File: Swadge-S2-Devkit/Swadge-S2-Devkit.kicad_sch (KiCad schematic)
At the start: 83 parts, among them J1 USB_B_Micro, J2 DEBUG_BANK_C, J3 DEBUG_BANK_B, J4 DEBUG_BANK_A, J5 MICSEL, J6 TRYMIC, M1 Motor_DC, Q1 Q_N_FET, Q2 AP2003_PN_FET, Q3 AP2003_PN_FET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

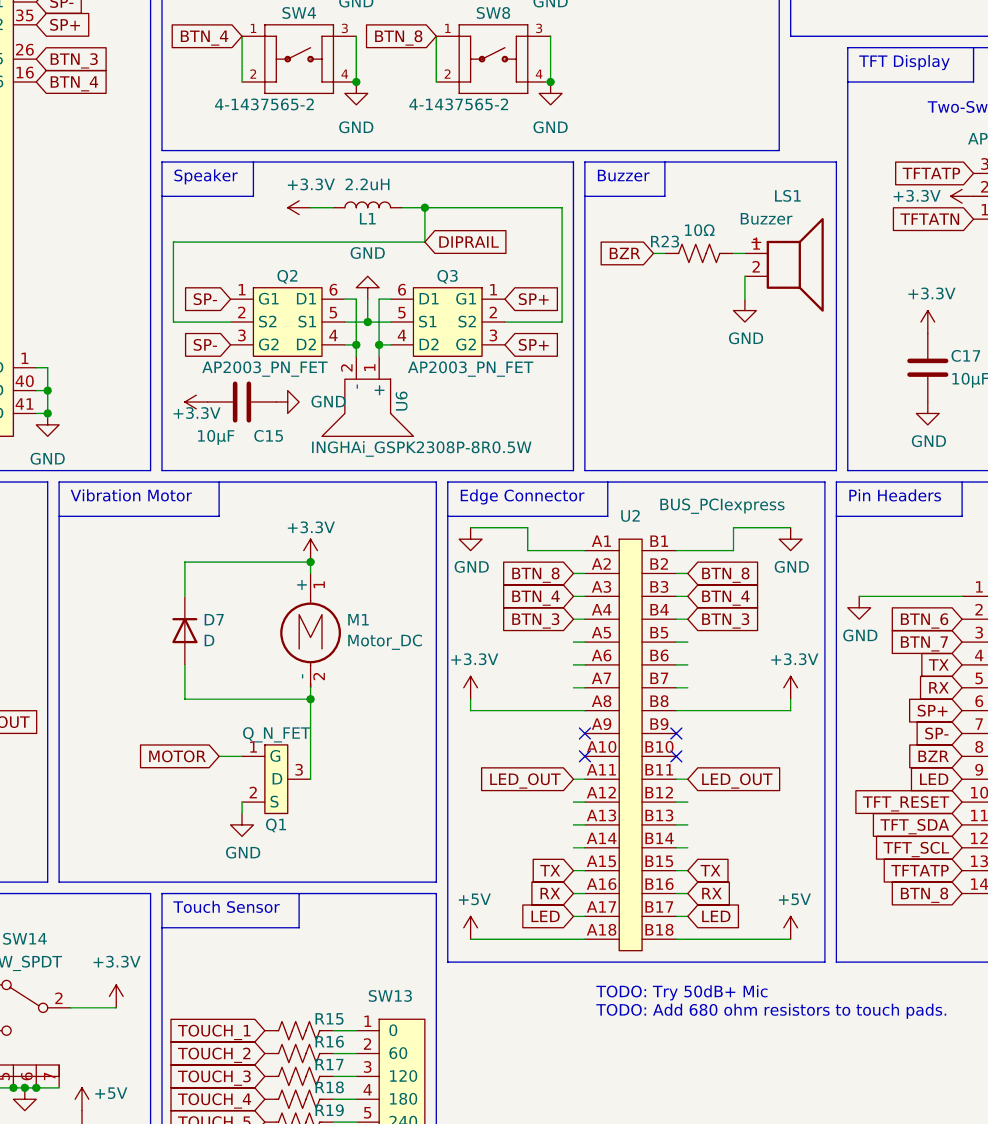
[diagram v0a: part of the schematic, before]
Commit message: Switched to controller PCB
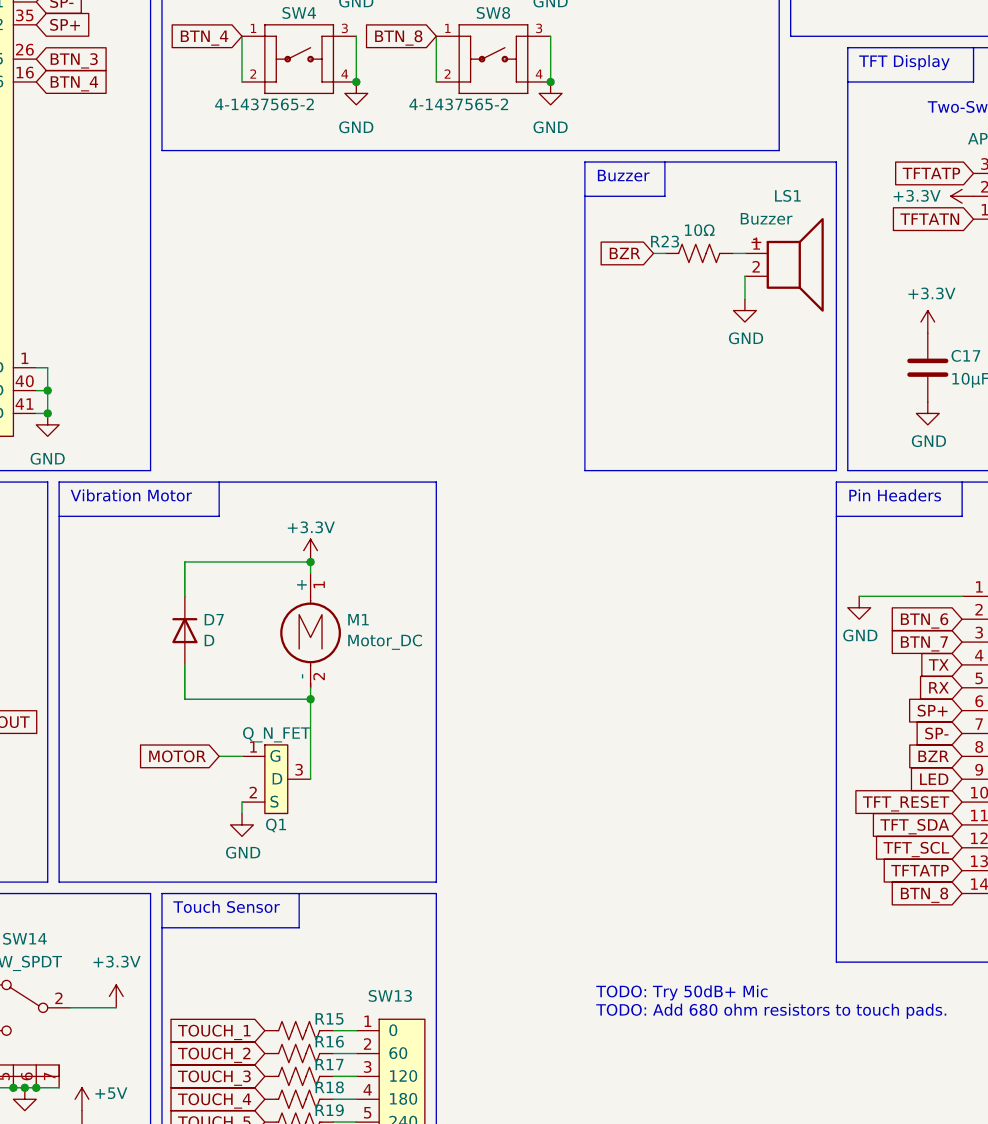
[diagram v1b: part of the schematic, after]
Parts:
- removed C15: 10μF, Swadge_Parts:C_0603_1608Metric, symbol Swadge_Parts:C
- removed L1: 2.2uH, Swadge_Parts:L_0603_1608Metric, symbol Swadge_Parts:L
- removed Q2, Q3: AP2003_PN_FET, Swadge_Parts:SOT-23-6, symbol Swadge_Parts:AP2003_PN_FET
- removed U2: BUS_PCIexpress, Swadge_Parts:BUS_PCIexpress, symbol Swadge_Parts:BUS_PCIexpress
- removed U6: INGHAi_GSPK2308P-8R0.5W, Swadge_Parts:INGHAi GSPK2308P-8R0.5W, symbol Swadge_Parts:INGHAi_GSPK2308P-8R0.5W
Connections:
- no-connect marks 8 -> 4
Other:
- note removed: "Edge Connector"
- note removed: "Speaker"
